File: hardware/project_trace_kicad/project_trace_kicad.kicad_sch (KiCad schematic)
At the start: 0 parts

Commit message: Draft Input Section
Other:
- added sheet Analog Anti-Aliasing Filter (AAAF.kicad_sch)
- added sheet Inputs (Inputs.kicad_sch)
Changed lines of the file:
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@@
 	(generator_version "9.0")
 	(paper "A4")
+	(sheet
+		(at 57.15 69.85)
+		(size 19.05 19.05)
+		(exclude_from_sim no)
+		(in_bom yes)
+		(on_board yes)
+		(dnp no)
+		(fields_autoplaced yes)
+		(stroke
+			(width 0.1524)
+			(type solid)
+			(color 0 0 0 0.6)
+		)
+		(fill
+			(color 215 236 255 1.0000)
+		)
+		(property "Sheetname" "Inputs"
+			(at 57.15 69.1384 0)
+			(effects
+				(font
+					(size 1.27 1.27)
+				)
+				(justify left bottom)
+			)
+		)
+		(property "Sheetfile" "Inputs.kicad_sch"
+			(at 57.15 89.4846 0)
+			(effects
+				(font
+					(size 1.27 1.27)
+				)
+				(justify left top)
+			)
+		)
+		(instances
+			(project "project_trace_kicad"
+				(path "/af51f4e5-b952-4b0e-baf2-78a72fb86fcd"
+					(page "2")
+				)
+			)
+		)
+	)
+	(sheet
+		(at 82.55 69.85)
+		(size 19.05 19.05)
+		(exclude_from_sim no)
+		(in_bom yes)
+		(on_board yes)
+		(dnp no)
+		(fields_autoplaced yes)
+		(stroke
+			(width 0.1524)
+			(type solid)
+			(color 0 0 0 0.6)
+		)
+		(fill
+			(color 215 236 255 1.0000)
+		)
+		(property "Sheetname" "Analog Anti-Aliasing Filter"
+			(at 82.55 69.1384 0)
+			(effects
+				(font
+					(size 1.27 1.27)
+				)
+				(justify left bottom)
+			)
+		)
+		(property "Sheetfile" "AAAF.kicad_sch"
+			(at 82.55 89.4846 0)
+			(effects
+				(font
+					(size 1.27 1.27)
+				)
+				(justify left top)
+			)
+		)
+		(instances
+			(project "project_trace_kicad"
+				(path "/af51f4e5-b952-4b0e-baf2-78a72fb86fcd"
+					(page "3")
+				)
+			)
+		)
+	)
 	(sheet_instances
 		(path "/"

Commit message: Rushed Push Footprint Lib
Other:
- removed sheet Analog Anti-Aliasing Filter
- added sheet Data Acquisition: AC (DAQ_AC.kicad_sch)
- added sheet Data Acquisition: DC (DAQ_DC.kicad_sch)
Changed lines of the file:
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@@
 	(paper "A4")
+	(sheet
+		(at 95.25 50.8)
+		(size 38.1 12.7)
+		(exclude_from_sim no)
+		(in_bom yes)
+		(on_board yes)
+		(dnp no)
+		(fields_autoplaced yes)
+		(stroke
+			(width 0.1524)
+			(type solid)
+			(color 0 0 0 0.6)
+		)
+		(fill
+			(color 215 236 255 1.0000)
+		)
+		(property "Sheetname" "Data Acquisition: DC"
+			(at 95.25 50.0884 0)
+			(effects
+				(font
+					(size 1.27 1.27)
+				)
+				(justify left bottom)
+			)
+		)
+		(property "Sheetfile" "DAQ_DC.kicad_sch"
+			(at 95.25 64.0846 0)
+			(effects
+				(font
+					(size 1.27 1.27)
+				)
+				(justify left top)
+			)
+		)
+		(instances
+			(project "project_trace_kicad"
+				(path "/af51f4e5-b952-4b0e-baf2-78a72fb86fcd"
+					(page "4")
+				)
+			)
+		)
+	)
 	(sheet
 		(at 57.15 69.85)
@@
 	)
 	(sheet
-		(at 82.55 69.85)
-		(size 19.05 19.05)
+		(at 95.25 82.55)
+		(size 38.1 12.7)
 		(exclude_from_sim no)
 		(in_bom yes)
@@
 			(color 215 236 255 1.0000)
 		)
-		(property "Sheetname" "Analog Anti-Aliasing Filter"
-			(at 82.55 69.1384 0)
+		(property "Sheetname" "Data Acquisition: AC"
+			(at 95.25 81.8384 0)
 			(effects
 				(font
@@
 			)
 		)
-		(property "Sheetfile" "AAAF.kicad_sch"
-			(at 82.55 89.4846 0)
+		(property "Sheetfile" "DAQ_AC.kicad_sch"
+			(at 95.25 95.8346 0)
 			(effects
 				(font

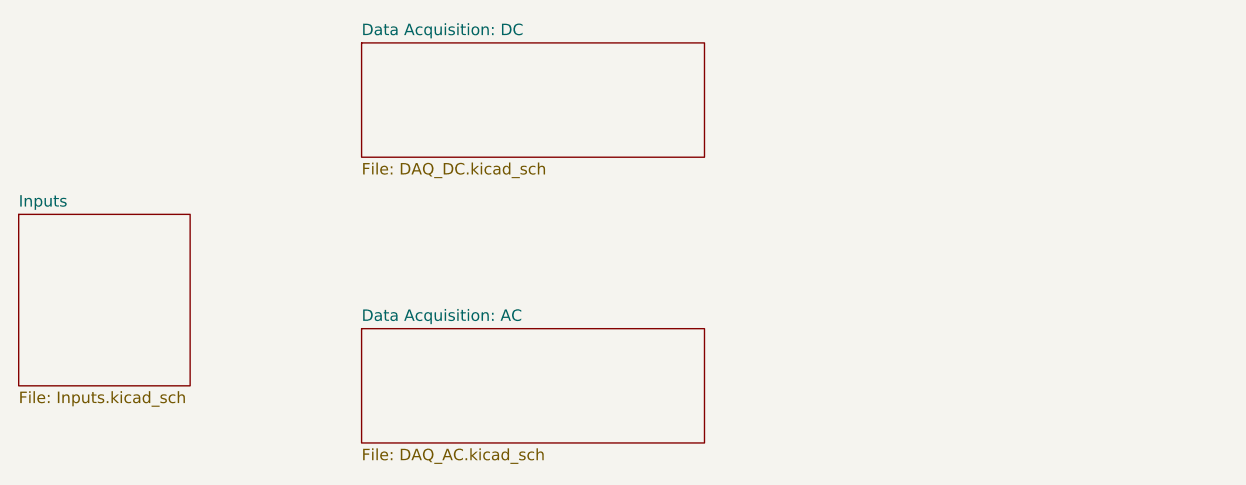
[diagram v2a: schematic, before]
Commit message: Create MAM Schematic
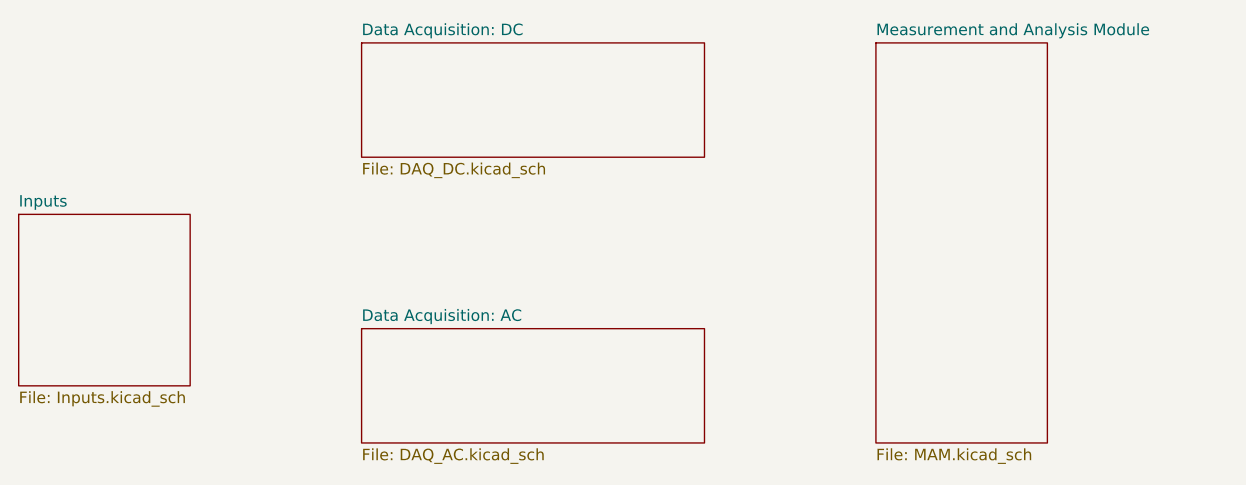
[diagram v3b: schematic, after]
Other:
- added sheet Measurement and Analysis Module (MAM.kicad_sch)
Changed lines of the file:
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@@
+		)
+	)
+	(sheet
+		(at 152.4 50.8)
+		(size 19.05 44.45)
+		(exclude_from_sim no)
+		(in_bom yes)
+		(on_board yes)
+		(dnp no)
+		(fields_autoplaced yes)
+		(stroke
+			(width 0.1524)
+			(type solid)
+			(color 0 0 0 0.6)
+		)
+		(fill
+			(color 215 236 255 1.0000)
+		)
+		(property "Sheetname" "Measurement and Analysis Module"
+			(at 152.4 50.0884 0)
+			(effects
+				(font
+					(size 1.27 1.27)
+				)
+				(justify left bottom)
+			)
+		)
+		(property "Sheetfile" "MAM.kicad_sch"
+			(at 152.4 95.8346 0)
+			(effects
+				(font
+					(size 1.27 1.27)
+				)
+				(justify left top)
+			)
+		)
+		(instances
+			(project "project_trace_kicad"
+				(path "/af51f4e5-b952-4b0e-baf2-78a72fb86fcd"
+					(page "5")
+				)
+			)
 		)
 	)
